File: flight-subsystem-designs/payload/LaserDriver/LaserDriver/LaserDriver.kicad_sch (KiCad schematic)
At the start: 43 parts, among them J1 Laser 0, J2 Laser 1, J3 Input, J4 BNC, U1 MAX3967AETG+, U2 DPC6137, U3 MAX3967AETG+, U4 74LVC1G04, U5 SY100ELT22ZG-TR

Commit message: laserdriver: finish routing (we're so back)
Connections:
- net ISO_SIGNAL_IN: now also U5.7 (D0)
- net SIGNAL_IN: no longer U5.7 (D0)
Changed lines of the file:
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@@
 	(wire
 		(pts
-			(xy 185.42 52.07) (xy 196.85 52.07)
+			(xy 182.88 52.07) (xy 196.85 52.07)
 		)
 		(stroke
@@
 		)
 	)
-	(label "SIGNAL_IN"
-		(at 185.42 52.07 0)
-		(effects
-			(font
+	(label "ISO_SIGNAL_IN"
+		(at 182.88 52.07 0)
+		(effects
+			(font

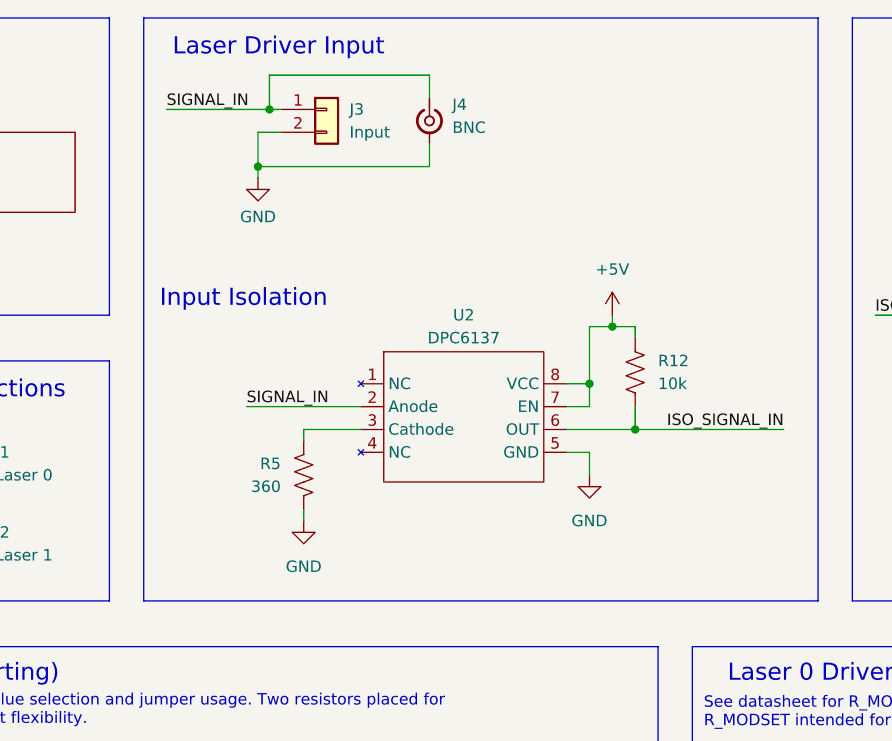
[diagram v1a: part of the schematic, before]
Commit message: laserdriver: signal gnd isolation; fix drcs; ready to export!
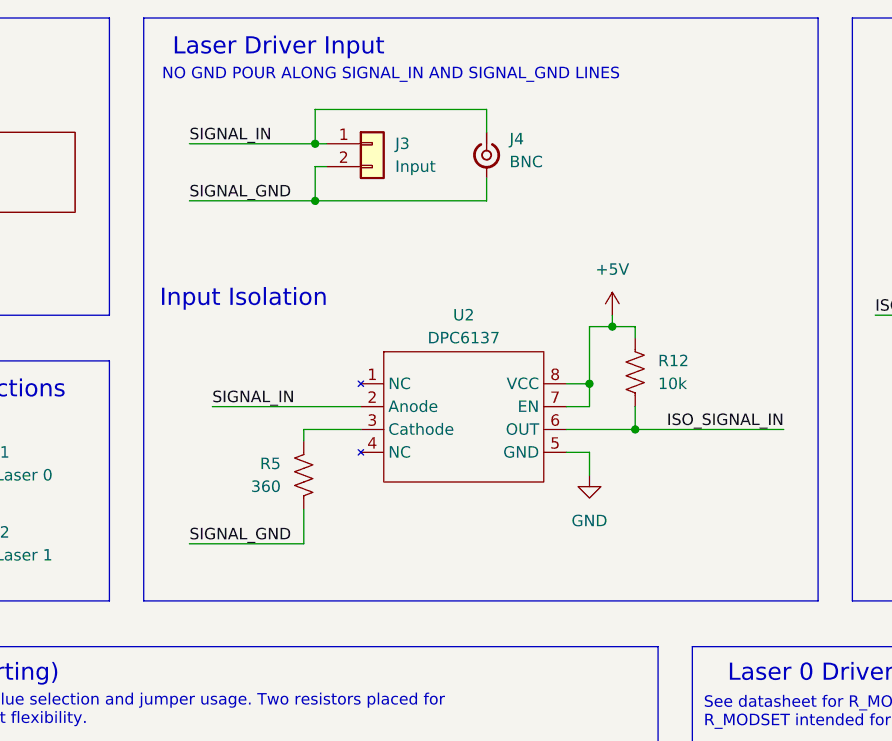
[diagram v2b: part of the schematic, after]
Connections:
- net GND: no longer J3.2 (Pin_2), J4.2 (Ext), R5.1
- new net SIGNAL_GND: J3.2 (Pin_2), J4.2 (Ext), R5.1
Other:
- note added: "NO GND POUR ALONG SIGNAL_IN AND SIGNAL_GND LINES"
- moved on the sheet: J3, J4
